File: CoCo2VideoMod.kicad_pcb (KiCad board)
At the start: 2 copper layers, 35 x 50 mm, 36 parts, among them J1 Conn_01x05, J2 Conn_01x03, J3 Conn_01x07, Q1 BC547, Q2 BC557, Q3 BC547, Q4 BC557, Q5 BC547, U1 MC1372P

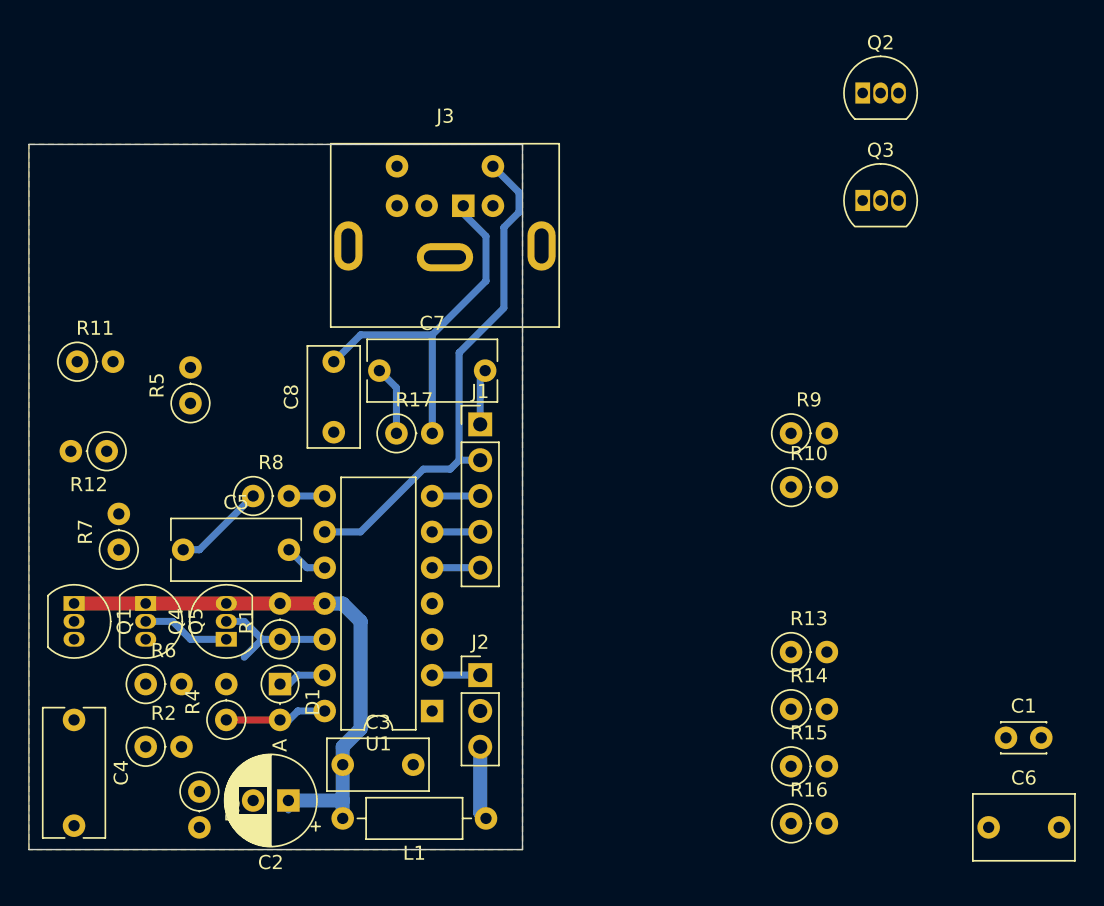
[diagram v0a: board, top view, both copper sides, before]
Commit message: croma and composite routing done
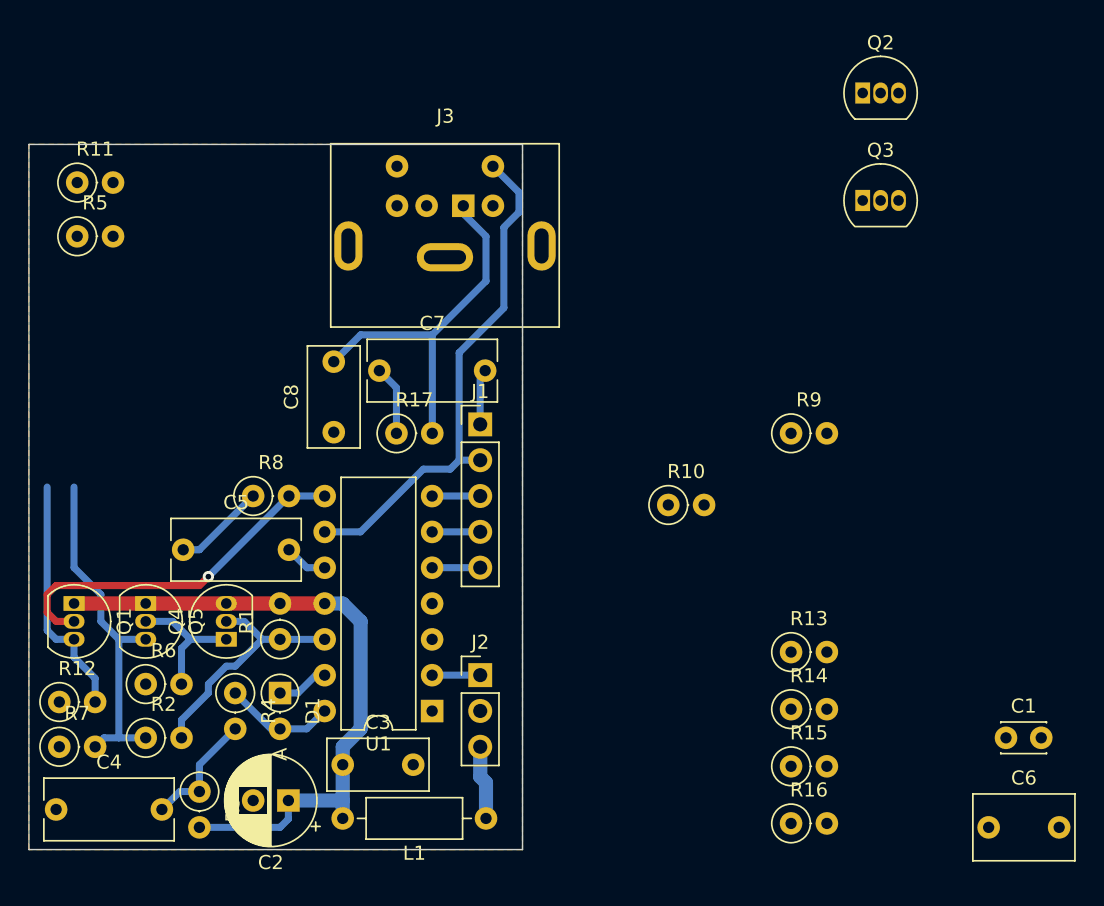
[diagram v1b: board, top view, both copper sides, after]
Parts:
- moved R12 18.1 mm to (202.2, 89.5), turned to 0 degrees
- moved R7 14.6 mm to (202.2, 92.7), turned to 0 degrees
- moved R5 14.3 mm to (203.4, 56.5), turned to 0 degrees
- moved R11 12.7 mm to (203.4, 52.7)
- moved R10 8.80 mm to (245.3, 75.6)
- moved C4 6.48 mm to (201.9, 97.2), turned to 0 degrees
- moved R4 2.01 mm to (214.6, 88.9), turned to -90 degrees
- moved D1 0.64 mm to (217.8, 88.9)
- moved R2 0.63 mm to (208.3, 92.1)
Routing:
- net Net-(Q5-E): track 0.00 -> 24.8 mm
- net Net-(Q1-B): track 2.54 -> 26.0 mm, vias 0 -> 1
- net Net-(Q1-E): track 0.00 -> 17.4 mm
- net Net-(C4-Pad2): track 0.00 -> 8.68 mm
- net Net-(Q4-B): track 9.30 -> 17.2 mm
- net +5V: track 39.9 -> 47.1 mm
- net Net-(Q4-C): track 6.24 -> 9.68 mm
- net Net-(D1-A): track 7.25 -> 7.92 mm

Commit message: midway chroma routing
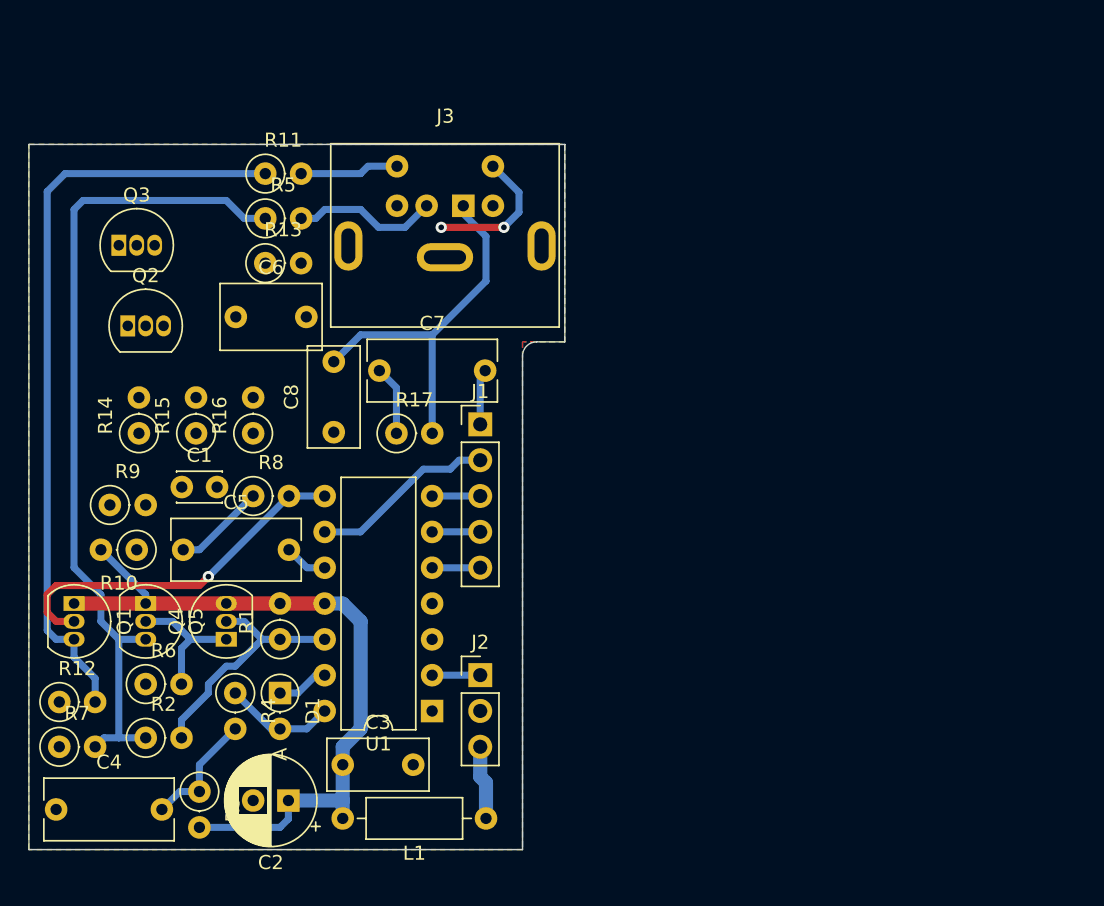
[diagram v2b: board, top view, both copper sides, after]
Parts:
- moved C6 64.5 mm to (214.7, 62.2)
- moved C1 61.1 mm to (210.8, 74.3)
- moved Q2 54.7 mm to (207.0, 62.9)
- moved Q3 52.8 mm to (206.4, 57.1)
- moved R14 50.2 mm to (207.8, 70.5), turned to 90 degrees
- moved R9 48.6 mm to (205.7, 75.6)
- moved R15 48.3 mm to (211.8, 70.5), turned to 90 degrees
- moved R16 47.1 mm to (215.9, 70.5), turned to 90 degrees
- moved R13 46.4 mm to (216.8, 58.4)
- moved R10 37.8 mm to (207.6, 78.7), turned to 180 degrees
- moved R5 13.4 mm to (216.8, 55.2)
- moved R11 13.4 mm to (216.8, 52.1)
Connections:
- net /Chroma renamed /Chroma_out
- net /V_comp renamed /Composite_out
- J3 pad 5: /Luma -> /Luma_out
- R13 pad 2: /Luma -> /Luma_out
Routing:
- net Net-(Q1-E): track 17.4 -> 54.3 mm
- net Net-(Q5-E): track 24.8 -> 58.9 mm
- net /Luma: track 36.5 -> 13.1 mm
- net /Composite_out: track 0.00 -> 10.3 mm
- net /Luma_out: track 0.00 -> 9.98 mm, vias 0 -> 2
- net /Chroma_out: track 0.00 -> 7.02 mm
- net +5V: track 47.1 -> 52.2 mm
- added copper zone on B.Cu, net GND
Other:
- board size 35 x 50 mm -> 38 x 50 mm

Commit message: on luma layout
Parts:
- moved R9 20.5 mm to (208.3, 55.2), turned to 180 degrees
- moved R15 14.8 mm to (214.0, 55.9), turned to 180 degrees
- moved R14 13.0 mm to (214.0, 59.1), turned to 180 degrees
- moved R16 8.57 mm to (218.2, 62.2), turned to 180 degrees
- moved C6 8.47 mm to (212.8, 70.5)
- moved Q3 8.35 mm to (205.1, 65.4)
- moved Q2 8.28 mm to (206.4, 71.1)
- moved C1 5.75 mm to (205.1, 74.9)
- moved R12 1.27 mm to (202.2, 88.3)
- moved C4 0.64 mm to (201.9, 96.5)
- moved C2 0.63 mm to (218.4, 95.9)
- moved R10 0.63 mm to (207.6, 78.1)
- moved R7 0.63 mm to (202.2, 92.1)
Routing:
- net /Luma_out: track 9.98 -> 24.7 mm, vias 2 -> 0
- net /Luma: track 13.1 -> 24.4 mm
- net Net-(Q2-E): track 0.00 -> 7.56 mm
- net +5V: track 52.2 -> 56.6 mm
- net Net-(Q1-E): track 54.3 -> 53.1 mm
- net /Audio out: track 26.2 -> 26.7 mm, vias 0 -> 1

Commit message: Layout complete
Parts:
- R8, R9: footprint Resistor_THT:R_Axial_DIN0207_L6.3mm_D2.5mm_P2.54mm_Vertical -> Resistor_THT:R_Axial_DIN0207_L6.3mm_D2.5mm_P7.62mm_Horizontal
- moved R9 11.1 mm to (212.7, 65.4)
- moved R16 11.0 mm to (209.6, 55.5), turned to -90 degrees
- moved R15 7.63 mm to (206.4, 55.5), turned to -90 degrees
- moved R14 7.29 mm to (217.6, 65.4)
- moved R8 5.12 mm to (210.8, 74.3)
- moved Q3 3.68 mm to (206.4, 62.0)
- moved C6 0.64 mm to (212.7, 69.8)
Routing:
- net Net-(Q2-C): track 0.00 -> 14.2 mm
- net +5V: track 56.6 -> 70.7 mm
- net Net-(Q2-B): track 0.00 -> 13.6 mm
- net Net-(Q3-E): track 0.00 -> 11.6 mm
- net /Luma: track 24.4 -> 21.8 mm
- net Net-(C5-Pad1): track 6.54 -> 4.66 mm
- net Net-(Q5-E): track 58.6 -> 59.5 mm
- net Net-(Q1-B): track 26.0 -> 26.9 mm
- net Net-(Q1-E): track 53.1 -> 53.6 mm

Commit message: silk screen complete
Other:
- board text added: "K"
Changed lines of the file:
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@@
     (property "ki_keywords" "cap capacitor")
     (attr through_hole)
-    (fp_text reference "C7" (at 3.75 -3.35) (layer "F.SilkS")
+    (fp_text reference "C7" (at 9.084 -1.778 -90) (layer "F.SilkS")
         (effects (font (size 1 1) (thickness 0.15)))
     )
@@
     (property "ki_keywords" "R res resistor")
     (attr through_hole)
-    (fp_text reference "R12" (at 1.27 -2.37) (layer "F.SilkS")
+    (fp_text reference "R12" (at 2.315 1.651) (layer "F.SilkS")
         (effects (font (size 1 1) (thickness 0.15)))
     )
@@
     (property "ki_keywords" "cap capacitor")
     (attr through_hole)
-    (fp_text reference "C1" (at 1.25 -2.25) (layer "F.SilkS")
+    (fp_text reference "C1" (at -2.56 0) (layer "F.SilkS")
         (effects (font (size 1 1) (thickness 0.15)))
     )
@@
     (property "ki_keywords" "cap capacitor")
     (attr through_hole)
-    (fp_text reference "C2" (at 1.25 -4.4) (layer "F.SilkS")
+    (fp_text reference "C2" (at -1.31 -3.175) (layer "F.SilkS")
         (effects (font (size 1 1) (thickness 0.15)))
     )
@@
     (property "Sheetname" "")
     (attr through_hole)
-    (fp_text reference "U1" (at 3.81 -2.33) (layer "F.SilkS")
+    (fp_text reference "U1" (at 3.81 7.625) (layer "F.SilkS")
         (effects (font (size 1 1) (thickness 0.15)))
     )
@@
     (property "ki_keywords" "R res resistor")
     (attr through_hole)
-    (fp_text reference "R15" (at 1.27 -2.37 -270) (layer "F.SilkS")
+    (fp_text reference "R15" (at -3.146 0 -270) (layer "F.SilkS")
         (effects (font (size 1 1) (thickness 0.15)))
     )
@@
     (property "ki_keywords" "R res resistor")
     (attr through_hole)
-    (fp_text reference "R17" (at 1.27 -2.37) (layer "F.SilkS")
+    (fp_text reference "R17" (at 2.54 1.905) (layer "F.SilkS")
         (effects (font (size 1 1) (thickness 0.15)))
     )
@@
     (property "ki_keywords" "inductor choke coil reactor magnetic")
     (attr through_hole)
-    (fp_text reference "L1" (at 5.08 -2.47) (layer "F.SilkS")
+    (fp_text reference "L1" (at 2.54 2.54) (layer "F.SilkS")
         (effects (font (size 1 1) (thickness 0.15)))
     )
@@
     (property "ki_keywords" "R res resistor")
     (attr through_hole)
-    (fp_text reference "R6" (at 1.27 -2.37) (layer "F.SilkS")
+    (fp_text reference "R6" (at 1.778 1.651) (layer "F.SilkS")
         (effects (font (size 1 1) (thickness 0.15)))
     )
@@
     (property "ki_keywords" "PNP Transistor")
     (attr through_hole)
-    (fp_text reference "Q4" (at 1.27 -3.56 90) (layer "F.SilkS")
+    (fp_text reference "Q4" (at 1.27 -3.937 90) (layer "F.SilkS")
         (effects (font (size 1 1) (thickness 0.15)))
     )
@@
     (property "ki_keywords" "R res resistor")
     (attr through_hole)
-    (fp_text reference "R7" (at 1.27 -2.37) (layer "F.SilkS")
+    (fp_text reference "R7" (at 1.807 1.651) (layer "F.SilkS")
         (effects (font (size 1 1) (thickness 0.15)))
     )
@@
     (property "ki_keywords" "diode")
     (attr through_hole)
-    (fp_text reference "D1" (at 1.27 -2.326371 90) (layer "F.SilkS")
+    (fp_text reference "D1" (at 1.27 -1.651 -90) (layer "F.SilkS")
         (effects (font (size 1 1) (thickness 0.15)))
     )
     (fp_text value "1N4148" (at 1.27 3.215371 90) (layer "F.Fab")
-        (effects (font (size 1 1) (thickness 0.15)))
-    )
-    (fp_text user "A" (at 4.34 0 90) (layer "F.SilkS")
         (effects (font (size 1 1) (thickness 0.15)))
     )
@@
     (property "ki_keywords" "NPN Transistor")
     (attr through_hole)
-    (fp_text reference "Q1" (at 1.27 -3.56 90) (layer "F.SilkS")
+    (fp_text reference "Q1" (at 1.27 -1.778 90) (layer "F.SilkS")
         (effects (font (size 1 1) (thickness 0.15)))
     )
@@
     (property "ki_keywords" "R res resistor")
     (attr through_hole)
-    (fp_text reference "R2" (at 1.27 -2.37) (layer "F.SilkS")
+    (fp_text reference "R2" (at 1.778 1.651) (layer "F.SilkS")
         (effects (font (size 1 1) (thickness 0.15)))
     )
@@
     (property "ki_keywords" "NPN Transistor")
     (attr through_hole)
-    (fp_text reference "Q5" (at 1.27 -3.56 90) (layer "F.SilkS")
+    (fp_text reference "Q5" (at 1.27 -4.064 90) (layer "F.SilkS")
         (effects (font (size 1 1) (thickness 0.15)))
     )
@@
     (property "ki_keywords" "R res resistor")
     (attr through_hole)
-    (fp_text reference "R9" (at 3.81 -2.37 180) (layer "F.SilkS")
+    (fp_text reference "R9" (at 1.397 2.159 180) (layer "F.SilkS")
         (effects (font (size 1 1) (thickness 0.15)))
     )
@@
     (property "ki_keywords" "R res resistor")
     (attr through_hole)
-    (fp_text reference "R10" (at 1.27 -2.37) (layer "F.SilkS")
+    (fp_text reference "R10" (at 5.08 0) (layer "F.SilkS")
         (effects (font (size 1 1) (thickness 0.15)))
     )
@@
     (property "ki_keywords" "cap capacitor")
     (attr through_hole)
-    (fp_text reference "C5" (at 3.75 -3.35) (layer "F.SilkS")
+    (fp_text reference "C5" (at -1.39 -2.794) (layer "F.SilkS")
         (effects (font (size 1 1) (thickness 0.15)))
     )
@@
     (property "ki_keywords" "R res resistor")
     (attr through_hole)
-    (fp_text reference "R13" (at 1.27 -2.37) (layer "F.SilkS")
+    (fp_text reference "R13" (at -3.146 0) (layer "F.SilkS")
         (effects (font (size 1 1) (thickness 0.15)))
     )
@@
     (property "ki_keywords" "cap capacitor")
     (attr through_hole)
-    (fp_text reference "C8" (at 2.5 -3 90) (layer "F.SilkS")
+    (fp_text reference "C8" (at 7.159 -1.397 90) (layer "F.SilkS")
         (effects (font (size 1 1) (thickness 0.15)))
     )
@@
     (property "ki_keywords" "cap capacitor")
     (attr through_hole)
-    (fp_text reference "C4" (at 3.75 -3.35) (layer "F.SilkS")
+    (fp_text reference "C4" (at 3.75 1.27) (layer "F.SilkS")
         (effects (font (size 1 1) (thickness 0.15)))
     )
@@
     (property "ki_keywords" "R res resistor")
     (attr through_hole)
-    (fp_text reference "R14" (at 1.27 -2.37) (layer "F.SilkS")
+    (fp_text reference "R14" (at 1.68 1.905) (layer "F.SilkS")
         (effects (font (size 1 1) (thickness 0.15)))
     )
@@
     (property "ki_keywords" "cap capacitor")
     (attr through_hole)
-    (fp_text reference "C3" (at 2.5 -3) (layer "F.SilkS")
+    (fp_text reference "C3" (at 6.985 -1.27 90) (layer "F.SilkS")
         (effects (font (size 1 1) (thickness 0.15)))
     )
@@
     (property "ki_keywords" "PNP Transistor")
     (attr through_hole)
-    (fp_text reference "Q2" (at 1.27 -3.56) (layer "F.SilkS")
+    (fp_text reference "Q2" (at -2.159 -1.905) (layer "F.SilkS")
         (effects (font (size 1 1) (thickness 0.15)))
     )
@@
     (property "ki_keywords" "connector")
     (attr through_hole)
-    (fp_text reference "J1" (at 0 -2.33) (layer "F.SilkS")
+    (fp_text reference "J1" (at 0 12.7 180) (layer "F.SilkS")
         (effects (font (size 1 1) (thickness 0.15)))
     )
@@
     (property "ki_keywords" "R res resistor")
     (attr through_hole)
-    (fp_text reference "R16" (at 1.27 -2.37 -270) (layer "F.SilkS")
+    (fp_text reference "R16" (at -3.146 0 -270) (layer "F.SilkS")
         (effects (font (size 1 1) (thickness 0.15)))
     )
@@
     (property "ki_keywords" "cap capacitor")
     (attr through_hole)
-    (fp_text reference "C6" (at 2.5 -3.5) (layer "F.SilkS")
+    (fp_text reference "C6" (at -2.159 -1.905) (layer "F.SilkS")
         (effects (font (size 1 1) (thickness 0.15)))
     )
@@
     (property "ki_keywords" "connector")
     (attr through_hole)
-    (fp_text reference "J3" (at -1.27 -6.35) (layer "F.SilkS")
+    (fp_text reference "J3" (at -1.565 -2.915) (layer "F.SilkS")
         (effects (font (size 1 1) (thickness 0.15)))
     )
@@
     (property "ki_keywords" "R res resistor")
     (attr through_hole)
-    (fp_text reference "R3" (at 1.27 -2.37 90) (layer "F.SilkS")
+    (fp_text reference "R3" (at -1.905 -0.635 -180) (layer "F.SilkS")
         (effects (font (size 1 1) (thickness 0.15)))
     )
@@
     (property "ki_keywords" "NPN Transistor")
     (attr through_hole)
-    (fp_text reference "Q3" (at 1.27 -3.56) (layer "F.SilkS")
+    (fp_text reference "Q3" (at -2.159 -1.63) (layer "F.SilkS")
         (effects (font (size 1 1) (thickness 0.15)))
     )
@@
     (property "ki_keywords" "R res resistor")
     (attr through_hole)
-    (fp_text reference "R5" (at 1.27 -2.37) (layer "F.SilkS")
+    (fp_text reference "R5" (at -2.638 0) (layer "F.SilkS")
         (effects (font (size 1 1) (thickness 0.15)))
     )
@@
     (property "ki_keywords" "R res resistor")
     (attr through_hole)
-    (fp_text reference "R1" (at 1.27 -2.37 90) (layer "F.SilkS")
+    (fp_text reference "R1" (at 1.524 1.651 180) (layer "F.SilkS")
         (effects (font (size 1 1) (thickness 0.15)))
     )
@@
     (property "ki_keywords" "R res resistor")
     (attr through_hole)
-    (fp_text reference "R11" (at 1.27 -2.37) (layer "F.SilkS")
+    (fp_text reference "R11" (at -2.892 0) (layer "F.SilkS")
         (effects (font (size 1 1) (thickness 0.15)))
     )
@@
     (property "ki_keywords" "R res resistor")
     (attr through_hole)
-    (fp_text reference "R4" (at 1.27 -2.37 90) (layer "F.SilkS")
+    (fp_text reference "R4" (at 1.778 1.524 90) (layer "F.SilkS")
         (effects (font (size 1 1) (thickness 0.15)))
     )
@@
     (property "ki_keywords" "R res resistor")
     (attr through_hole)
-    (fp_text reference "R8" (at 3.81 -2.37) (layer "F.SilkS")
+    (fp_text reference "R8" (at 8.89 -1.27) (layer "F.SilkS")
         (effects (font (size 1 1) (thickness 0.15)))
     )
@@
   (gr_line (start 235 100) (end 235 65)
     (stroke (width 0.1) (type default)) (layer "Edge.Cuts"))
+  (gr_text "K" (at 219.964 88.138 90) (layer "F.SilkS")
+    (effects (font (size 1 1) (thickness 0.15)) (justify left bottom))
+  )
   (segment (start 205.125 73.045) (end 204.47 72.39) (width 1) (layer "F.Cu") (net 1))
   (segment (start 204.47 69.85) (end 205.105 69.215) (width 1) (layer "F.Cu") (net 1))

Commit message: fab complete
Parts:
- J1: value Conn_01x05 -> 20261043
- J2: value Conn_01x03 -> to PCB
- J3: value Conn_01x07 -> Video
